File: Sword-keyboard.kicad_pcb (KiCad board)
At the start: 2 copper layers, 130.5 x 107.5 mm, 48 parts, among them J1 STX-3000, SW1 SW_Push, SW10 SW_Push, SW12 SW_Push, SW13 SW_Push, SW14 SW_Push, SW15 SW_Push, SW16 SW_Push, SW17 SW_Push, SW19 SW_Push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

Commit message: Exchanged audio jack
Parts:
- J1: value STX-3000 -> SJ1-3523N; footprint KiCADv6:STX-3000_KYC -> kicad:CUI_SJ1-3523N
- SW11: value (none) -> SW_Push
- moved J1 5.00 mm to (94.0, 116.5), turned to -90 degrees
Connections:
- J1 pad 2: GND -> VCC
- J1 pad 3: VCC -> GND
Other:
- outline, holes or cut-outs redrawn

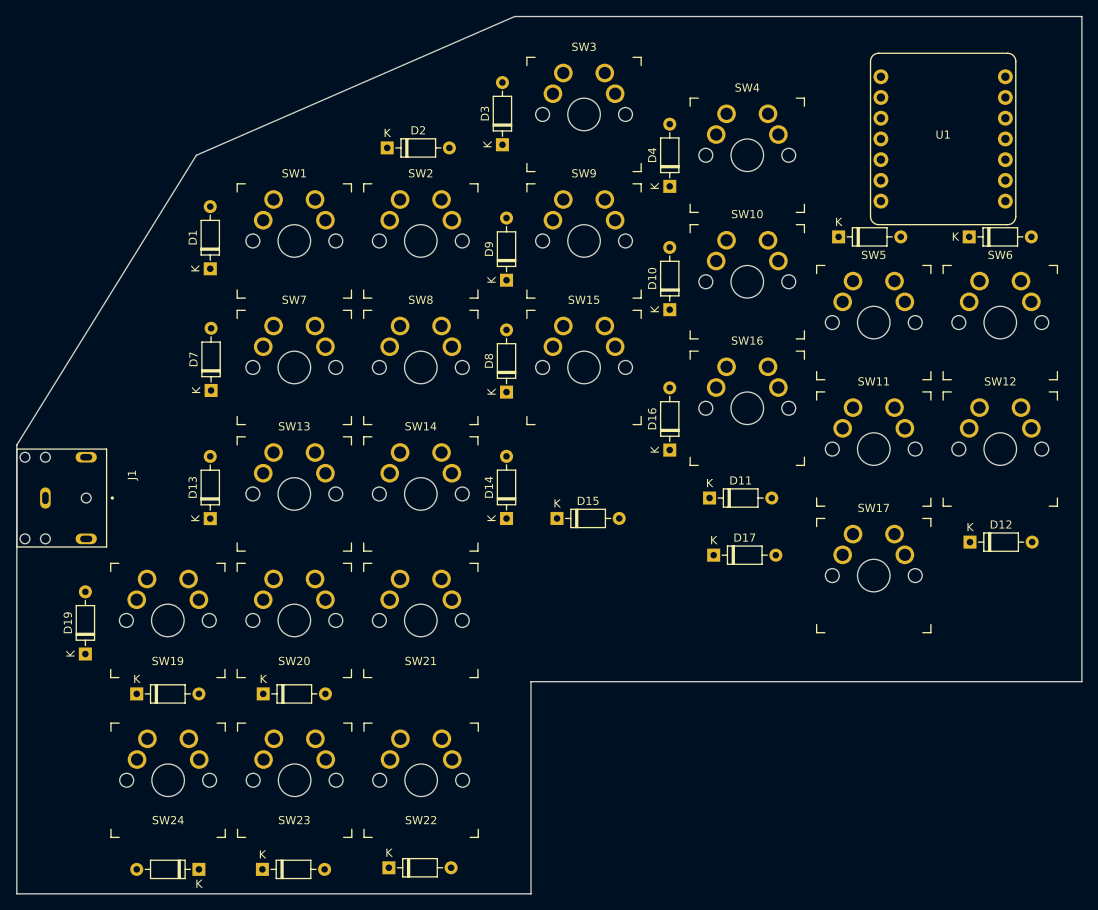
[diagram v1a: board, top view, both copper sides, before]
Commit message: Reduced the outline of the board a little.
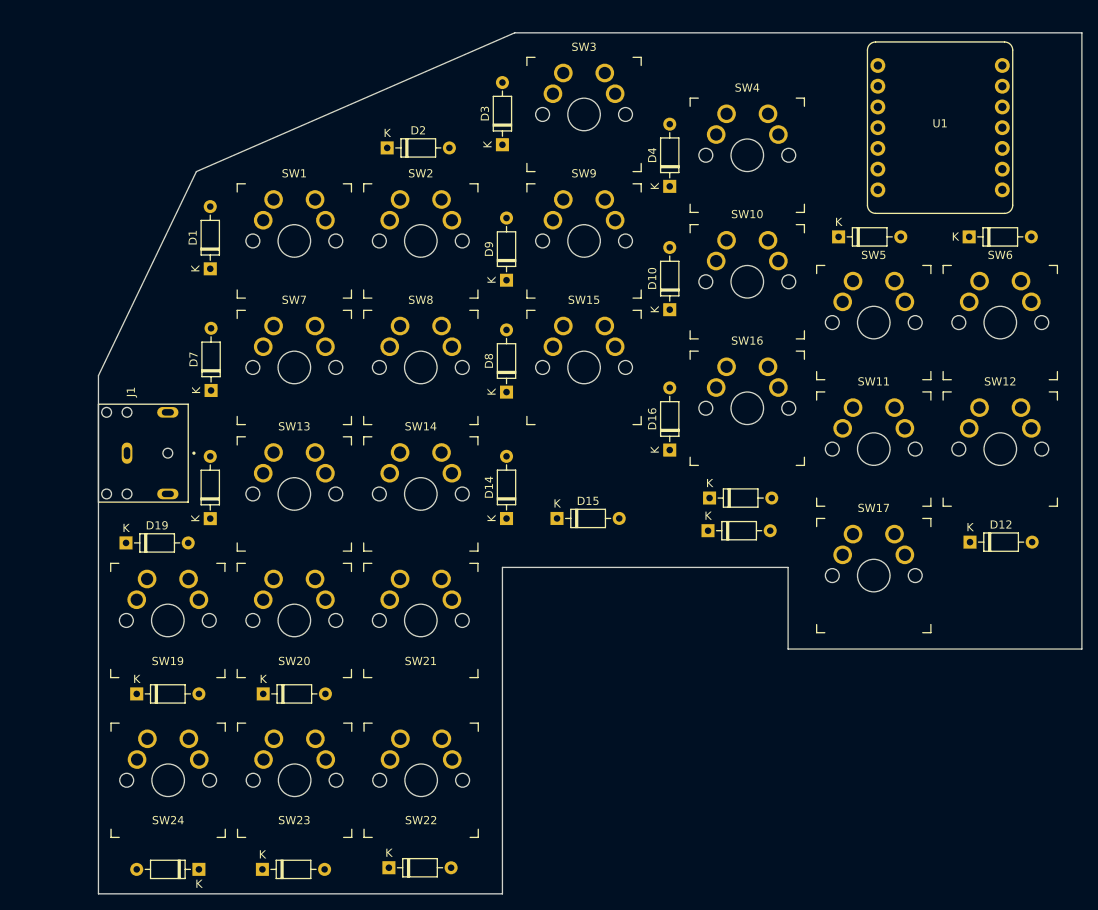
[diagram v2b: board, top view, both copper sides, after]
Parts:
- moved D19 14.5 mm to (103.9, 122.0), turned to 0 degrees
- moved J1 11.4 mm to (104.0, 111.0)
- moved D17 3.08 mm to (175.2, 120.5)
- moved U1 1.43 mm to (203.6, 71.1)
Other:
- board size 130.5 x 107.5 mm -> 120.5 x 105.5 mm
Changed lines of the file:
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@@
 			(at 3.81 -2.12 -90)
 			(layer "F.SilkS")
+			(hide yes)
 			(effects
 				(font
@@
 	(footprint "Diode_THT:D_DO-35_SOD27_P7.62mm_Horizontal"
 		(layer "F.Cu")
-		(at 98.9 135.61 90)
+		(at 103.88 122)
 		(descr "Diode, DO-35_SOD27 series, Axial, Horizontal, pin pitch=7.62mm, , length*diameter=4*2mm^2, , http://www.diodes.com/_files/packages/DO-35.pdf")
 		(tags "Diode DO-35_SOD27 series Axial Horizontal pin pitch 7.62mm  length 4mm diameter 2mm")
 		(property "Reference" "D19"
-			(at 3.81 -2.12 -90)
+			(at 3.81 -2.12 360)
 			(layer "F.SilkS")
 			(effects
@@
 		)
 		(property "Value" "1N4148"
-			(at 3.81 2.12 -90)
+			(at 3.81 2.12 360)
 			(layer "F.Fab")
 			(hide yes)
@@
 		)
 		(property "Footprint" "Diode_THT:D_DO-35_SOD27_P7.62mm_Horizontal"
-			(at 0 0 90)
+			(at 0 0 0)
 			(unlocked yes)
 			(layer "F.Fab")
@@
 		)
 		(property "Datasheet" "https://assets.nexperia.com/documents/data-sheet/1N4148_1N4448.pdf"
-			(at 0 0 90)
+			(at 0 0 0)
 			(unlocked yes)
 			(layer "F.Fab")
@@
 		)
 		(property "Description" "100V 0.15A standard switching diode, DO-35"
-			(at 0 0 90)
+			(at 0 0 0)
 			(unlocked yes)
 			(layer "F.Fab")
@@
 		)
 		(property "Sim.Device" "D"
-			(at 0 0 90)
+			(at 0 0 0)
 			(unlocked yes)
 			(layer "F.Fab")
@@
 		)
 		(property "Sim.Pins" "1=K 2=A"
-			(at 0 0 90)
+			(at 0 0 0)
 			(unlocked yes)
 			(layer "F.Fab")
@@
 		(attr through_hole)
 		(fp_line
-			(start 5.93 -1.12)
-			(end 1.69 -1.12)
+			(start 1.04 0)
+			(end 1.69 0)
 			(stroke
 				(width 0.12)
@@
 		)
 		(fp_line
-			(start 2.53 -1.12)
-			(end 2.53 1.12)
+			(start 1.69 -1.12)
+			(end 1.69 1.12)
 			(stroke
 				(width 0.12)
@@
 		)
 		(fp_line
-			(start 2.41 -1.12)
-			(end 2.41 1.12)
+			(start 1.69 1.12)
+			(end 5.93 1.12)
 			(stroke
 				(width 0.12)
@@
 		)
 		(fp_line
-			(start 1.69 -1.12)
-			(end 1.69 1.12)
+			(start 2.41 -1.12)
+			(end 2.41 1.12)
 			(stroke
 				(width 0.12)
@@
 		)
 		(fp_line
-			(start 6.58 0)
-			(end 5.93 0)
+			(start 2.53 -1.12)
+			(end 2.53 1.12)
 			(stroke
 				(width 0.12)
@@
 		)
 		(fp_line
-			(start 1.04 0)
-			(end 1.69 0)
+			(start 5.93 -1.12)
+			(end 1.69 -1.12)
 			(stroke
 				(width 0.12)
@@
 		)
 		(fp_line
-			(start 1.69 1.12)
-			(end 5.93 1.12)
+			(start 6.58 0)
+			(end 5.93 0)
 			(stroke
 				(width 0.12)
@@
 		)
 		(fp_line
-			(start 8.67 -1.25)
-			(end -1.05 -1.25)
+			(start -1.05 -1.25)
+			(end -1.05 1.25)
 			(stroke
 				(width 0.05)
@@
 		)
 		(fp_line
-			(start -1.05 -1.25)
-			(end -1.05 1.25)
+			(start -1.05 1.25)
+			(end 8.67 1.25)
 			(stroke
 				(width 0.05)
@@
 		)
 		(fp_line
-			(start 8.67 1.25)
-			(end 8.67 -1.25)
+			(start 8.67 -1.25)
+			(end -1.05 -1.25)
 			(stroke
 				(width 0.05)
@@
 		)
 		(fp_line
-			(start -1.05 1.25)
-			(end 8.67 1.25)
+			(start 8.67 1.25)
+			(end 8.67 -1.25)
 			(stroke
 				(width 0.05)
@@
 		)
 		(fp_line
-			(start 5.81 -1)
-			(end 1.81 -1)
+			(start 0 0)
+			(end 1.81 0)
 			(stroke
 				(width 0.1)
@@
 		)
 		(fp_line
-			(start 2.51 -1)
-			(end 2.51 1)
+			(start 1.81 -1)
+			(end 1.81 1)
 			(stroke
 				(width 0.1)
@@
 		)
 		(fp_line
-			(start 2.41 -1)
-			(end 2.41 1)
+			(start 1.81 1)
+			(end 5.81 1)
 			(stroke
 				(width 0.1)
@@
 		)
 		(fp_line
-			(start 1.81 -1)
-			(end 1.81 1)
+			(start 2.41 -1)
+			(end 2.41 1)
 			(stroke
 				(width 0.1)
@@
 		)
 		(fp_line
-			(start 7.62 0)
-			(end 5.81 0)
+			(start 2.51 -1)
+			(end 2.51 1)
 			(stroke
 				(width 0.1)
@@
 		)
 		(fp_line
-			(start 0 0)
-			(end 1.81 0)
+			(start 5.81 -1)
+			(end 1.81 -1)
 			(stroke
 				(width 0.1)
@@
 		)
 		(fp_line
-			(start 1.81 1)
-			(end 5.81 1)
+			(start 7.62 0)
+			(end 5.81 0)
 			(stroke
 				(width 0.1)
@@
 		)
 		(fp_text user "K"
-			(at 0 -1.8 -90)
+			(at 0 -1.8 360)
 			(layer "F.SilkS")
 			(effects
@@
 		)
 		(fp_text user "${REFERENCE}"
-			(at 4.11 0 -90)
+			(at 4.11 0 360)
 			(layer "F.Fab")
 			(effects
@@
 		)
 		(fp_text user "K"
-			(at 0 -1.8 -90)
+			(at 0 -1.8 360)
 			(layer "F.Fab")
 			(effects
@@
 		)
 		(pad "1" thru_hole rect
-			(at 0 0 90)
+			(at 0 0)
 			(size 1.6 1.6)
 			(drill 0.8)
@@
 		)
 		(pad "2" thru_hole oval
-			(at 7.62 0 90)
+			(at 7.62 0)
 			(size 1.6 1.6)
 			(drill 0.8)
@@
 	(footprint "kicad:CUI_SJ1-3523N"
 		(layer "F.Cu")
-		(at 94 116.5 -90)
+		(at 104 111 -90)
 		(property "Reference" "J1"
-			(at -2.825 -10.635 90)
+			(at -7.5 -0.5 90)
 			(layer "F.SilkS")
 			(effects
@@
 			(at 2.255 -9.135 90)
 			(layer "F.Fab")
+			(hide yes)
 			(effects
 				(font
@@
 	(footprint "Diode_THT:D_DO-35_SOD27_P7.62mm_Horizontal"
 		(layer "F.Cu")
-		(at 175.88 123.5)
+		(at 175.19 120.5)
 		(descr "Diode, DO-35_SOD27 series, Axial, Horizontal, pin pitch=7.62mm, , length*diameter=4*2mm^2, , http://www.diodes.com/_files/packages/DO-35.pdf")
 		(tags "Diode DO-35_SOD27 series Axial Horizontal pin pitch 7.62mm  length 4mm diameter 2mm")
@@
 			(at 3.81 -2.12 0)
 			(layer "F.SilkS")
+			(hide yes)
 			(effects
 				(font
@@
 	(footprint "Seeeduino-XIAO:Seeed XIAO RP2040"
 		(layer "F.Cu")
-		(at 204 72.5)
+		(at 203.625 71.12)
 		(property "Reference" "U1"
 			(at 0 -0.5 0)
@@
 			(at 3.81 -2.12 0)
 			(layer "F.SilkS")
+			(hide yes)
 			(effects
 				(font
@@
 	)
 	(gr_line
-		(start 221 139)
-		(end 153.5 139)
+		(start 221 135)
+		(end 185 135)
+		(stroke
+			(width 0.05)
+			(type default)
+		)
+		(layer "Edge.Cuts")
+	)
+	(gr_line
+		(start 221 59.5)
+		(end 221 135)
+		(stroke
+			(width 0.05)
+			(type default)
+		)
+		(layer "Edge.Cuts")
+	)
+	(gr_line
+		(start 150 125)
+		(end 150 165)
 		(stroke
 			(width 0.05)
@@
 	)
 	(gr_line
-		(start 221 57.5)
-		(end 221 139)
+		(start 100.5 101.5)
+		(end 112.5 76.5)
 		(stroke
 			(width 0.05)
@@
 	)
 	(gr_line
-		(start 153.5 139)
-		(end 153.5 165)
+		(start 100.5 165)
+		(end 100.5 101.5)
 		(stroke
 			(width 0.05)
@@
 	)
 	(gr_line
-		(start 90.5 110)
-		(end 112.5 74.5)
+		(start 185 125)
+		(end 185 135)
 		(stroke
 			(width 0.05)
@@
 	)
 	(gr_line
-		(start 90.5 165)
-		(end 90.5 110)
+		(start 150 165)
+		(end 100.5 165)
 		(stroke
 			(width 0.05)
@@
 	)
 	(gr_line
-		(start 153.5 165)
-		(end 90.5 165)
+		(start 151.5 59.5)
+		(end 221 59.5)
 		(stroke
 			(width 0.05)
@@
 	)
 	(gr_line
-		(start 151.5 57.5)
-		(end 221 57.5)
+		(start 112.5 76.5)
+		(end 151.5 59.5)
 		(stroke
 			(width 0.05)
@@
 	)
 	(gr_line
-		(start 112.5 74.5)
-		(end 151.5 57.5)
+		(start 150 125)
+		(end 185 125)
 		(stroke
 			(width 0.05)

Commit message: Routed everything.
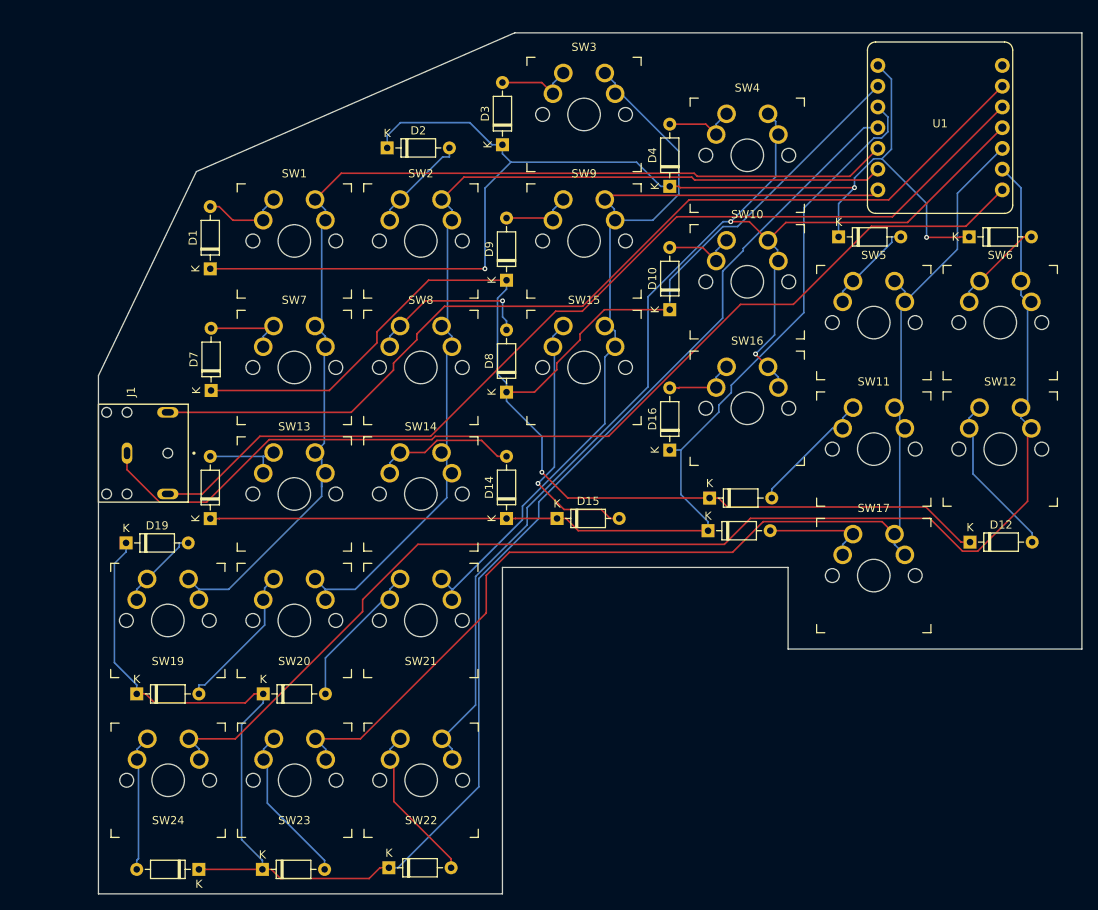
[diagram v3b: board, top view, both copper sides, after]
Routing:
- net row3: track 0.00 -> 201.7 mm
- net row1: track 0.00 -> 188.9 mm, vias 0 -> 1
- net col5: track 0.00 -> 165.6 mm
- net col3: track 0.00 -> 158.7 mm, vias 0 -> 2
- net row0: track 0.00 -> 153.5 mm, vias 0 -> 3
- net col4: track 0.00 -> 148.4 mm
- net col0: track 0.00 -> 135.3 mm
- net row2: track 0.00 -> 127.8 mm
- net DATA: track 0.00 -> 126.8 mm
- net col2: track 0.00 -> 123.0 mm
- net VCC: track 0.00 -> 121.9 mm
- net GND: track 0.00 -> 119.7 mm
- net col1: track 0.00 -> 117.4 mm
- net Net-(D15-A): track 0.00 -> 32.5 mm, vias 0 -> 1
- net Net-(D8-A): track 0.00 -> 20.7 mm, vias 0 -> 1
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
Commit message: Added silkscreen logo
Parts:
- added G***: LOGO, Sword-keyboard:sword-logo, F.Cu at (211.5, 128.0)
- added G***: LOGO, Sword-keyboard:sword-logo, B.Cu at (211.5, 128.0)
